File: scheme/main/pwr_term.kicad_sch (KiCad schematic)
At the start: 1 part, among them J1 DG45C-B-06P-13-00A

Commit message: added L fuse & more
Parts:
- added F1: Fuse, symbol Device:Fuse
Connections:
- net L: now also F1.2; no longer J1.3 (Pin_3)
- new net: F1.1, J1.3 (Pin_3)
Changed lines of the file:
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@@
+	(wire
+		(pts
+			(xy 163.83 102.87) (xy 158.75 102.87)
+		)
+		(stroke
+			(width 0)
+			(type default)
+		)
+	)
 	(wire
 		(pts
@@
 	(wire
 		(pts
-			(xy 176.53 102.87) (xy 158.75 102.87)
+			(xy 171.45 102.87) (xy 176.53 102.87)
 		)
 		(stroke
@@
 		)
 	)
+	(symbol
+		(lib_id "Device:Fuse")
+		(at 167.64 102.87 90)
+		(unit 1)
+		(exclude_from_sim no)
+		(in_bom yes)
+		(on_board yes)
+		(dnp no)
+		(property "Reference" "F1"
+			(at 167.64 109.22 90)
+			(effects
+				(font
+					(size 1.27 1.27)
+				)
+			)
+		)
+		(property "Value" "Fuse"
+			(at 167.64 106.68 90)
+			(effects
+				(font
+					(size 1.27 1.27)
+				)
+			)
+		)
+		(property "Footprint" ""
+			(at 167.64 104.648 90)
+			(effects
+				(font
+					(size 1.27 1.27)
+				)
+				(hide yes)
+			)
+		)
+		(property "Datasheet" "~"
+			(at 167.64 102.87 0)
+			(effects
+				(font
+					(size 1.27 1.27)
+				)
+				(hide yes)
+			)
+		)
+		(property "Description" "Fuse"
+			(at 167.64 102.87 0)
+			(effects
+				(font
+					(size 1.27 1.27)
+				)
+				(hide yes)
+			)
+		)
+		(pin "2"
+		)
+		(pin "1"
+		)
+		(instances
+			(project ""
+				(path "/c11d1dbc-4db9-4712-8d1d-5f6f7086cded/95789226-49ac-48bd-87d5-f3fb8512f467"
+					(reference "F1")
+					(unit 1)
+				)
+			)
+		)
+	)

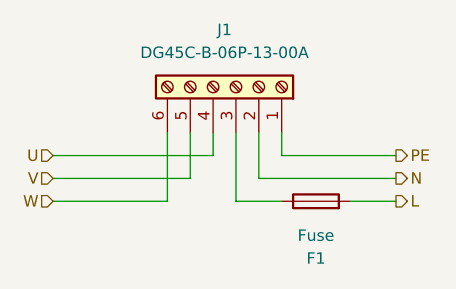
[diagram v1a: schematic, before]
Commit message: added 24V & GND to DO terminal & more
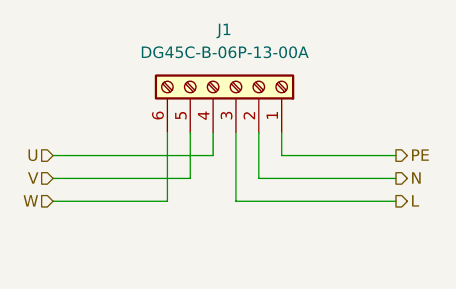
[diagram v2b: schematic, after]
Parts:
- removed F1: Fuse, symbol Device:Fuse
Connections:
- net L: now also J1.3 (Pin_3)
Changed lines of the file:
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@@
 	(wire
 		(pts
-			(xy 163.83 102.87) (xy 158.75 102.87)
+			(xy 158.75 102.87) (xy 176.53 102.87)
 		)
 		(stroke
@@
 		(pts
 			(xy 161.29 100.33) (xy 161.29 95.25)
-		)
-		(stroke
-			(width 0)
-			(type default)
-		)
-	)
-	(wire
-		(pts
-			(xy 171.45 102.87) (xy 176.53 102.87)
 		)
 		(stroke
@@
 		)
 	)
-	(symbol
-		(lib_id "Device:Fuse")
-		(at 167.64 102.87 90)
-		(unit 1)
-		(exclude_from_sim no)
-		(in_bom yes)
-		(on_board yes)
-		(dnp no)
-		(property "Reference" "F1"
-			(at 167.64 109.22 90)
-			(effects
-				(font
-					(size 1.27 1.27)
-				)
-			)
-		)
-		(property "Value" "Fuse"
-			(at 167.64 106.68 90)
-			(effects
-				(font
-					(size 1.27 1.27)
-				)
-			)
-		)
-		(property "Footprint" ""
-			(at 167.64 104.648 90)
-			(effects
-				(font
-					(size 1.27 1.27)
-				)
-				(hide yes)
-			)
-		)
-		(property "Datasheet" "~"
-			(at 167.64 102.87 0)
-			(effects
-				(font
-					(size 1.27 1.27)
-				)
-				(hide yes)
-			)
-		)
-		(property "Description" "Fuse"
-			(at 167.64 102.87 0)
-			(effects
-				(font
-					(size 1.27 1.27)
-				)
-				(hide yes)
-			)
-		)
-		(pin "2"
-		)
-		(pin "1"
-		)
-		(instances
-			(project ""
-				(path "/c11d1dbc-4db9-4712-8d1d-5f6f7086cded/95789226-49ac-48bd-87d5-f3fb8512f467"
-					(reference "F1")
-					(unit 1)
-				)
-			)
-		)
-	)

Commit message: sheets titles
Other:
- title: (none) -> Силовой клеммник
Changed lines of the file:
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@@
 	(generator_version "8.0")
 	(paper "A4")
+	(title_block
+		(title "Силовой клеммник")
+	)
 	(wire
 		(pts
